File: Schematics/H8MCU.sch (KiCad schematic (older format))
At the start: 4 parts

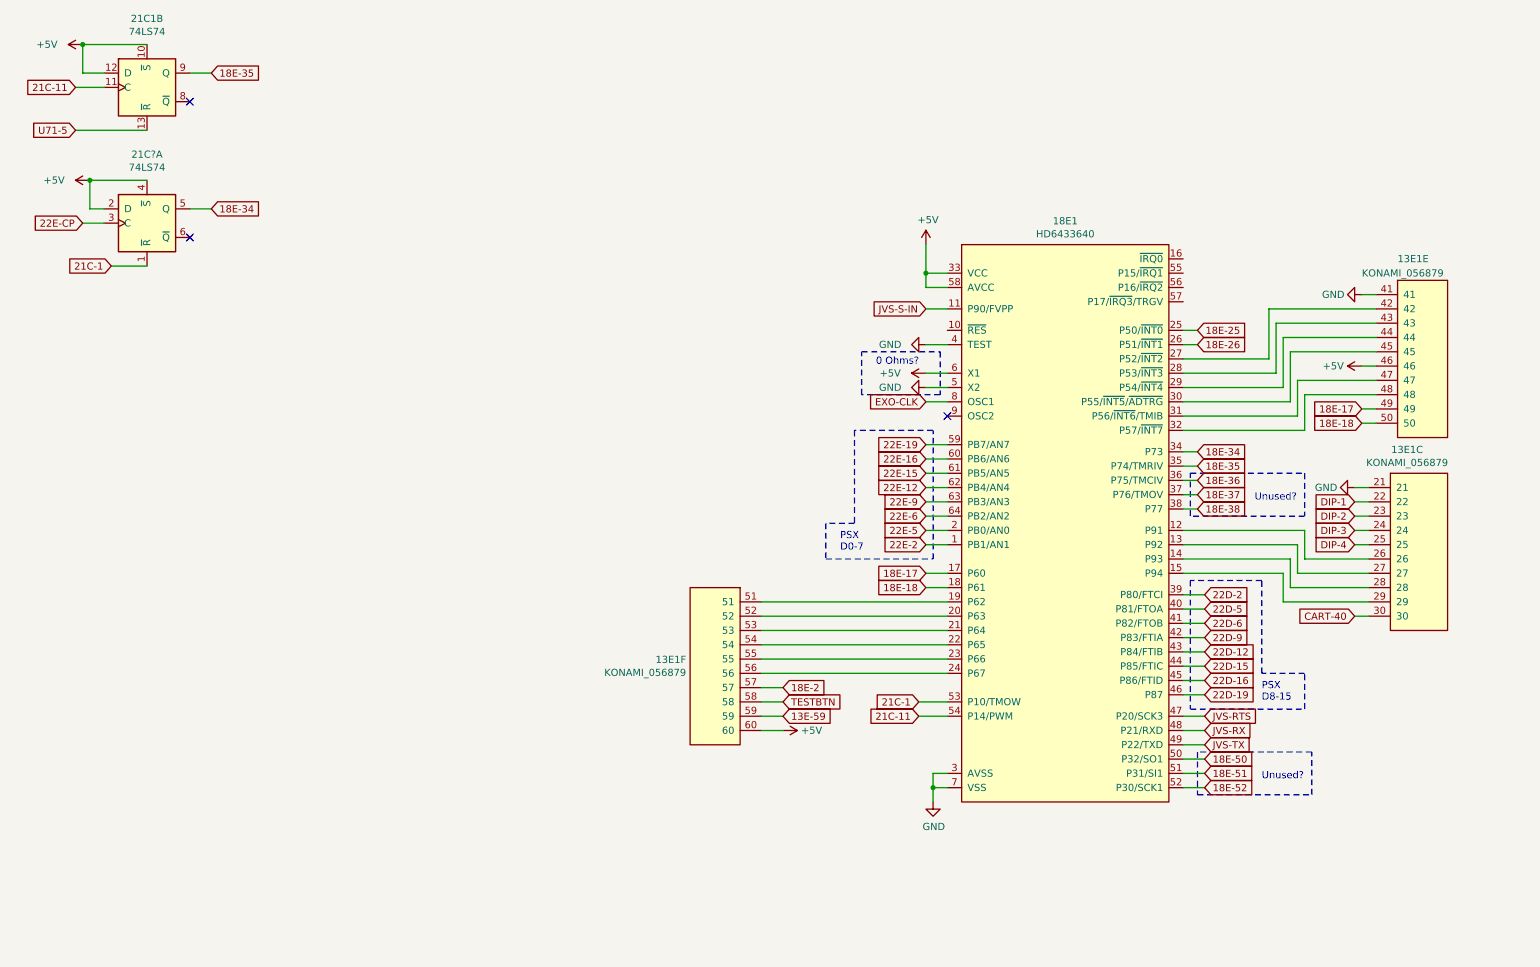
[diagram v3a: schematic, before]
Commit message: Flash fixes, security cart done, most logic figured
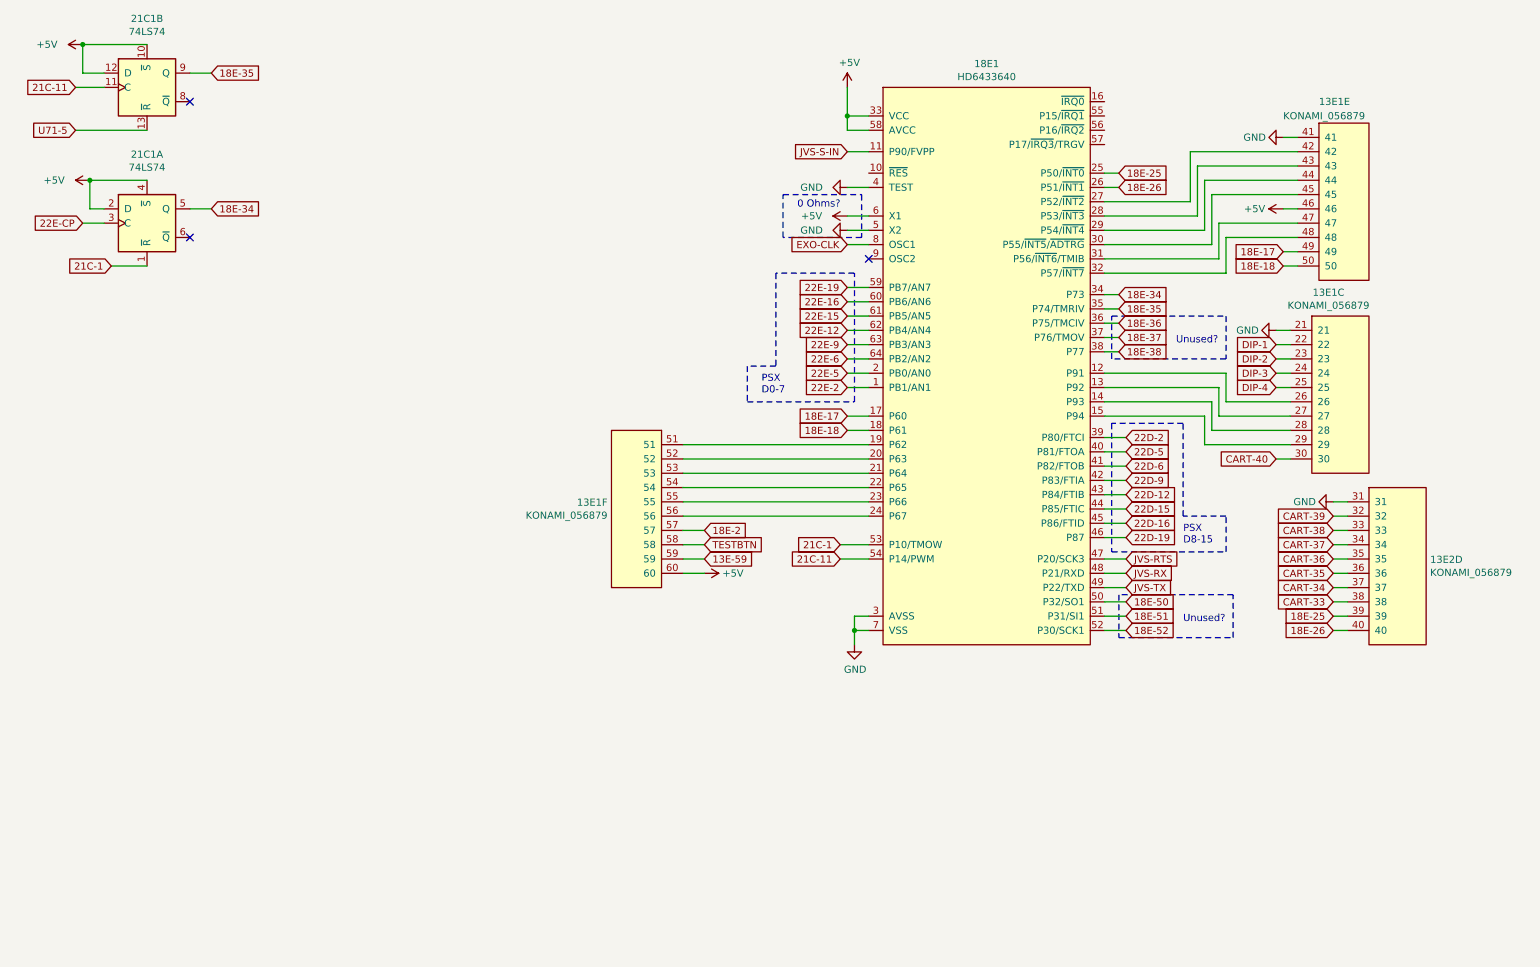
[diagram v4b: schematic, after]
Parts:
- added 13E2: KONAMI_056879, Package_QFP:TQFP-120_14x14mm_P0.4mm, symbol Arcade:KONAMI_056879
- gave numbers to parts that had none: 1
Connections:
- net 18E-25: now also 13E2.39
- net 18E-26: now also 13E2.40
- net GND: now also 13E2.31
- new net CART-33: 13E2.38
- new net CART-34: 13E2.37
- new net CART-35: 13E2.36
- new net CART-36: 13E2.35
- new net CART-37: 13E2.34
- new net CART-38: 13E2.33
- new net CART-39: 13E2.32
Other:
- moved on the sheet: 13E1C, 13E1E, 13E1F, 18E1

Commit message: 573 specific mostly mapped
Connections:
- net 18E-2 is gone; now on an unnamed net: 13E1.57
- net GND: now also 13E1.51
- net H8-~RST: now reaches 18E1.10 (~RES)
- net 18E-16: now reaches 18E1.16 (~IRQ0)
- net at 18E1.19 (P62): now also 13E1.52; no longer 13E1.51
- net at 18E1.20 (P63): now also 13E1.53; no longer 13E1.52
- net at 18E1.21 (P64): now also 13E1.54; no longer 13E1.53
- net at 18E1.22 (P65): now also 13E1.55; no longer 13E1.54
- net at 18E1.23 (P66): now also 13E1.56; no longer 13E1.55
- net at 18E1.24 (P67): no longer 13E1.56
- net 18E-55: now reaches 18E1.55 (P15/~IRQ1)
- net 18E-56: now reaches 18E1.56 (P16/~IRQ2)
- net 18E-57: now reaches 18E1.57 (P17/~IRQ3~/TRGV)
- net 18E-25: no longer names the net of 13E2.39, 18E1.25 (P50/~INT0)
- net 18E-26: no longer names the net of 13E2.40, 18E1.26 (P51/~INT1)
- net 21C-11 renamed 18E-54
- net 22E-CP renamed U71-39
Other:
- note added: "16-Bit input port"
- note added: "16-Bit output HI?"
- note added: "16-Bit output LO?"
- note added: "Am told the firmware does not use these"
- note added: "JVS"
- note added: "Latched Data\nD0-7"
- note added: "Latched Data\nD8-15"
- note added: "Status output flags?"
- note added: "Unused,\nPulled\nhigh"
- note removed: "0 Ohms?"
- note removed: "PSX\nD0-7"
- note removed: "PSX\nD8-15"
- note removed: "Unused?"
- moved on the sheet: 13E1C, 13E1E, 13E1F, 13E2D, 18E1, 21C1A, 21C1B
